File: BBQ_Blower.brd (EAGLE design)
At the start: 84.9 x 75.9 mm, 29 parts, among them IC1 MAX31855RASA+, IC2 MAX31855RASA+, IC3 MAX31855RASA+, J1 PCC-SMP-K-100-R-ROHS, J3 PCC-SMP-K-100-R-ROHS, J4 PCC-SMP-K-100-R-ROHS, Q1 BUZ10, Q2 BUZ10

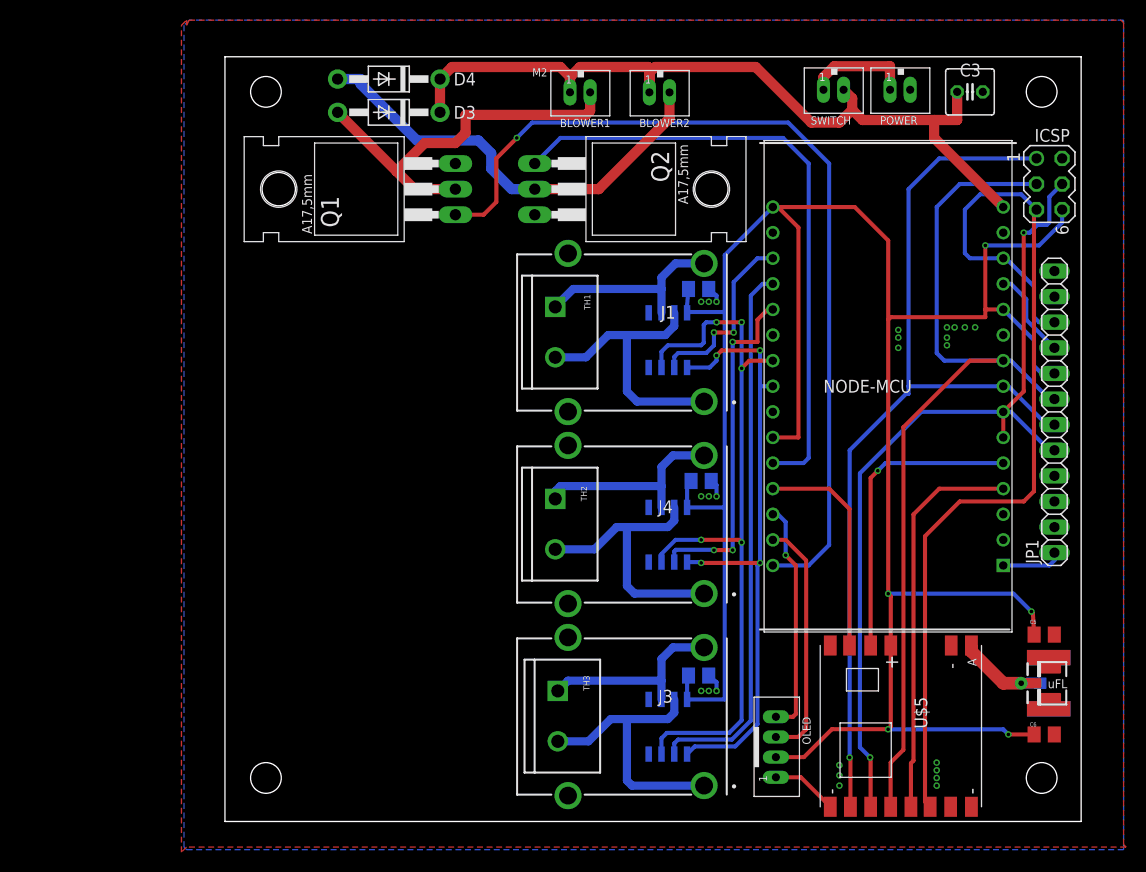
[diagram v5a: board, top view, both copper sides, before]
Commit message: rounded corners
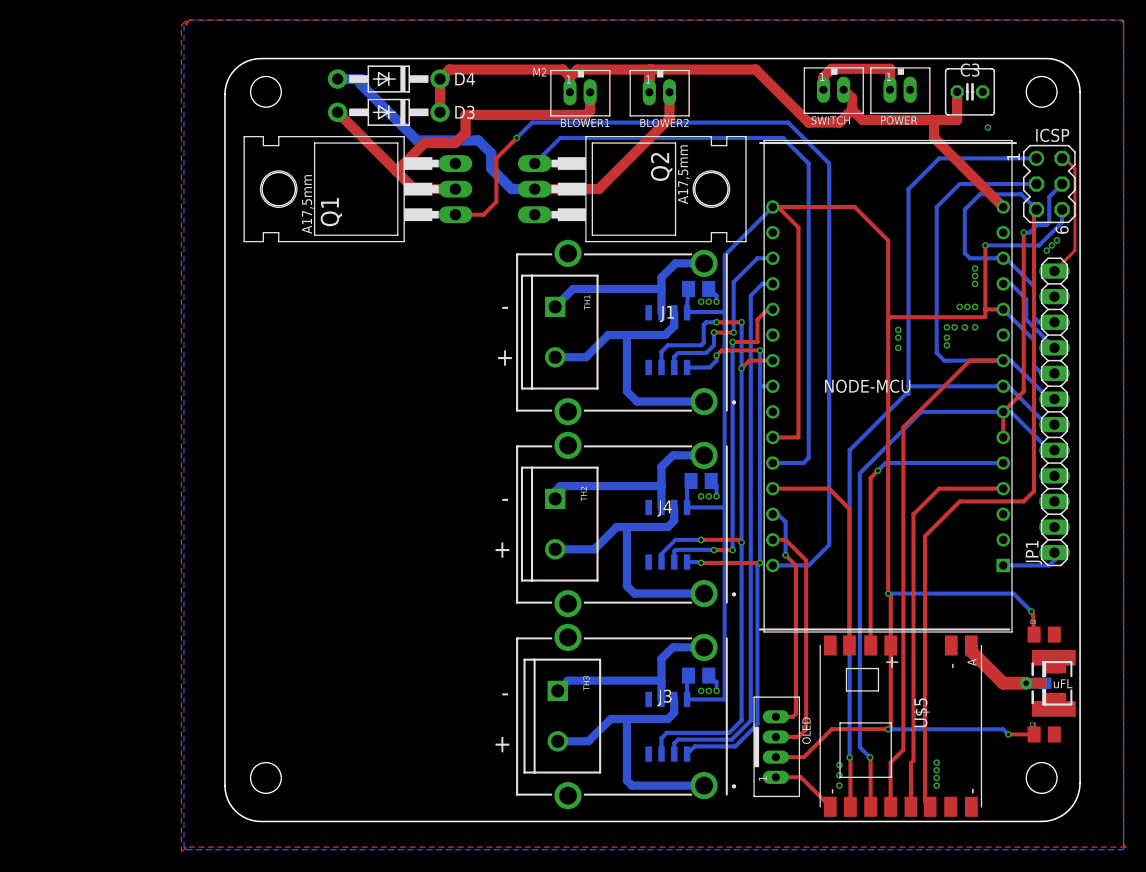
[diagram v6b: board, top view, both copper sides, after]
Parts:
- moved J$2 0.51 mm to (89.9, 17.8)
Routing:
- net GND: track 14.2 -> 26.9 mm, vias 25 -> 35
- net VDD: track 83.4 -> 82.7 mm
- net ANT: track 9.56 -> 10.1 mm
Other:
- board size 84.9 x 75.9 mm -> 84.8 x 75.7 mm

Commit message: first final
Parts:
- added R1, R2: 4.7K, _c2h:0805-RES
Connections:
- net 3V3: now also R1.2, R2.2
- net SCL: now also R1.1
- net SDA: now also R2.1
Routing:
- net 3V3: track 240.1 -> 245.0 mm, vias 5 -> 6
- net SDA: track 23.2 -> 25.2 mm, vias 1 -> 2
- net SCL: track 24.2 -> 25.3 mm, vias 0 -> 1
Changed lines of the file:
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@@
 </variantdefs>
 <classes>
-<class number="0" name="default" width="0.3048" drill="0.3556">
-<clearance class="0" value="0.254"/>
+<class number="0" name="default" width="0.2032" drill="0.3556">
+<clearance class="0" value="0.1524"/>
 </class>
 <class number="1" name="POWER" width="1.905" drill="0">
@@
 <attribute name="NAME" x="67.441" y="74.0255" size="0.8128" layer="25" font="vector" rot="R180"/>
 </element>
+<element name="R1" library="_c2h" package="0805-RES" value="4.7K" x="65.024" y="16.002" smashed="yes" rot="MR180">
+<attribute name="NAME" x="64.262" y="15.1765" size="0.4064" layer="26" rot="MR180"/>
+<attribute name="VALUE" x="64.008" y="17.399" size="0.4064" layer="28" rot="MR180"/>
+</element>
+<element name="R2" library="_c2h" package="0805-RES" value="4.7K" x="65.024" y="18.034" smashed="yes" rot="MR180">
+<attribute name="NAME" x="64.262" y="17.2085" size="0.4064" layer="26" rot="MR180"/>
+<attribute name="VALUE" x="64.008" y="19.431" size="0.4064" layer="28" rot="MR180"/>
+</element>
 </elements>
 <signals>
@@
 <contactref element="OLED" pad="P2"/>
 <wire x1="59.9915" y1="10.45" x2="62.774" y2="10.45" width="0.4064" layer="1"/>
-<wire x1="65.548" y1="13.224" x2="71.136" y2="13.224" width="0.4064" layer="1"/>
+<wire x1="65.548" y1="13.224" x2="66.04" y2="13.224" width="0.4064" layer="1"/>
+<wire x1="66.04" y1="13.224" x2="71.136" y2="13.224" width="0.4064" layer="1"/>
 <wire x1="62.774" y1="10.45" x2="65.548" y2="13.224" width="0.4064" layer="1"/>
+<contactref element="R2" pad="2"/>
+<contactref element="R1" pad="2"/>
+<wire x1="66.024" y1="18.034" x2="66.024" y2="16.002" width="0.4064" layer="16"/>
+<wire x1="66.024" y1="16.002" x2="66.024" y2="13.224" width="0.4064" layer="16"/>
+<wire x1="66.024" y1="13.224" x2="66.04" y2="13.208" width="0.4064" layer="16"/>
+<wire x1="66.04" y1="13.208" x2="66.04" y2="13.224" width="0.4064" layer="16"/>
+<via x="66.04" y="13.224" extent="1-16" drill="0.3556"/>
 </signal>
 <signal name="A0">
@@
 <wire x1="59.69" y1="32.004" x2="60.96" y2="32.004" width="0.4064" layer="1"/>
 <wire x1="60.96" y1="32.004" x2="62.992" y2="29.972" width="0.4064" layer="1"/>
-<wire x1="62.992" y1="29.972" x2="62.992" y2="13.208" width="0.4064" layer="1"/>
+<wire x1="62.992" y1="29.972" x2="62.992" y2="16.002" width="0.4064" layer="1"/>
+<wire x1="62.992" y1="16.002" x2="62.992" y2="13.208" width="0.4064" layer="1"/>
 <wire x1="62.234" y1="12.45" x2="59.9915" y2="12.45" width="0.4064" layer="1"/>
 <wire x1="62.992" y1="13.208" x2="62.234" y2="12.45" width="0.4064" layer="1"/>
+<contactref element="R1" pad="1"/>
+<via x="62.992" y="16.002" extent="1-16" drill="0.3556"/>
+<wire x1="64.024" y1="16.002" x2="62.992" y2="16.002" width="0.4064" layer="16"/>
 </signal>
 <signal name="SDA">
@@
 <wire x1="59.9915" y1="14.45" x2="61.694" y2="14.45" width="0.4064" layer="1"/>
 <wire x1="61.694" y1="14.45" x2="61.976" y2="14.732" width="0.4064" layer="1"/>
-<wire x1="61.976" y1="14.732" x2="61.976" y2="29.464" width="0.4064" layer="1"/>
+<wire x1="61.976" y1="14.732" x2="61.976" y2="18.034" width="0.4064" layer="1"/>
+<wire x1="61.976" y1="18.034" x2="61.976" y2="29.464" width="0.4064" layer="1"/>
 <wire x1="61.976" y1="29.464" x2="60.96" y2="30.48" width="0.4064" layer="1"/>
 <via x="60.96" y="30.48" extent="1-16" drill="0.3556"/>
@@
 <wire x1="60.96" y1="33.782" x2="60.198" y2="34.544" width="0.4064" layer="16"/>
 <wire x1="60.198" y1="34.544" x2="59.69" y2="34.544" width="0.4064" layer="16"/>
+<contactref element="R2" pad="1"/>
+<wire x1="64.024" y1="18.034" x2="61.976" y2="18.034" width="0.4064" layer="16"/>
+<via x="61.976" y="18.034" extent="1-16" drill="0.3556"/>
 </signal>
 <signal name="VIN">
